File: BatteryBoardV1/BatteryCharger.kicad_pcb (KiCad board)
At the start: 2 copper layers, 49.5 x 50.8 mm, 12 parts, among them U1 MCP73213

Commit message: Add files via upload
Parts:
- removed PROG1: TP5, Wire_Pads:SolderWirePad_single_1-2mmDrill
- removed R3: 2.37K, Resistors_SMD:R_0603_HandSoldering
- removed STAT1: TP6, Wire_Pads:SolderWirePad_single_1-2mmDrill
- added Q1: Q_NMOS_GSD, TO_SOT_Packages_SMD:SOT-23, F.Cu at (142.2, 104.1)
- JIn1: footprint BJCs:DC_2.1mm_CUI-PJ-202A -> Connectors:Barrel_Jack_CUI_PJ-102AH
- R1: value 2.37K -> 1.185K
- moved R2 62.8 mm to (166.4, 98.4)
- moved JOut1 57.1 mm to (150.5, 109.9)
- moved JIn2 55.8 mm to (146.7, 82.5), turned to 0 degrees
- moved C1 54.3 mm to (142.2, 99.1)
- moved R1 54.3 mm to (158.1, 96.5)
- moved U1 54.2 mm to (150.5, 97.8)
- moved C2 54.0 mm to (141.6, 92.7)
- moved JIn1 50.0 mm to (165.7, 90.2)
- moved D1 39.4 mm to (150.5, 92.7), turned to 180 degrees
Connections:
- U1 pad 9: GND -> Net-(U1-Pad9)
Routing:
- net VDD: track 71.0 -> 5.75 mm, vias 0 -> 1
- net Net-(D1-Pad1): track 7.63 -> 20.1 mm
- net Net-(PROG1-Pad1): track 7.68 -> 0.00 mm
- net GND: track 33.1 -> 25.7 mm, vias 6 -> 10
- net Net-(R2-Pad1): track 19.7 -> 12.7 mm
- net Net-(R1-Pad1): track 8.64 -> 4.53 mm
- added copper zone on F.Cu, net VDD
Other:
- board size 49.5 x 50.8 mm -> 33.7 x 41.3 mm
- net class High Current added: clearance 0.2, trace_width 0.5, via_dia 0.6, via_drill 0.4
- net class Less High Current added: clearance 0.2, trace_width 0.3, via_dia 0.6, via_drill 0.4

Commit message: Add files via upload
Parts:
- added J1: Conn_01x04_Male, Connector_Molex:Molex_Micro-Fit_3.0_43045-0412_2x02_P3.00mm_Vertical, F.Cu at (153.4, 107.7)
- D1: footprint LEDs:LED_0603_HandSoldering -> LEDs:LED_0805_HandSoldering
- JIn2, JOut1: footprint Connectors_Terminal_Blocks:TerminalBlock_Altech_AK300-2_P5.00mm -> TerminalBlock_Phoenix:TerminalBlock_Phoenix_PT-1,5-2-5.0-H_1x02_P5.00mm_Horizontal
- R1: value 1.185K -> 3K; footprint Resistors_SMD:R_0603_HandSoldering -> Resistors_SMD:R_0805_HandSoldering
- R2: footprint Resistors_SMD:R_0603_HandSoldering -> Resistors_SMD:R_0805_HandSoldering
- U1: footprint Housings_SSOP:MSOP-10-1EP_3x3mm_Pitch0.5mm -> Housings_DFN_QFN:DFN-10-1EP_3x3mm_Pitch0.5mm
- moved JIn2 15.4 mm to (132.1, 87.4)
- moved U1 13.0 mm to (137.7, 100.1)
- moved R2 12.6 mm to (153.9, 100.6)
- moved C1 12.4 mm to (130.0, 101.1)
- moved Q1 12.1 mm to (130.6, 107.2)
- moved C2 11.9 mm to (130.0, 95.5)
- moved R1 11.5 mm to (146.8, 98.6)
- moved D1 9.68 mm to (141.2, 95.5)
- moved JIn1 9.55 mm to (156.5, 87.9), turned to 270 degrees
- moved JOut1 8.81 mm to (141.7, 110.7), turned to 180 degrees
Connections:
- net Net-(C1-Pad1) renamed /VBAT+
- JOut1 pad 2: GND -> /VBAT-
- Q1 pad 3: GND -> /VBAT-
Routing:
- net /VBAT+: track 20.2 -> 32.1 mm
- net /VBAT-: track 0.00 -> 8.14 mm
- net GND: track 25.7 -> 21.0 mm, vias 10 -> 13
- net VDD: track 5.75 -> 2.00 mm
- net Net-(D1-Pad1): track 20.1 -> 17.0 mm
- net Net-(R1-Pad1): track 4.53 -> 6.46 mm
- net Net-(R2-Pad1): track 12.7 -> 13.4 mm
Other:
- board size 33.7 x 41.3 mm -> 32.5 x 33.5 mm

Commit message: Add files via upload
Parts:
- J1: footprint Connector_Molex:Molex_Micro-Fit_3.0_43045-0412_2x02_P3.00mm_Vertical -> SOAR_Library:Molex_Micro-Fit_3.0_43045-0400_2x02_P3.00mm_Horizontal
- moved JIn1 14.3 mm to (142.2, 89.4), turned to 90 degrees
- moved J1 8.87 mm to (151.4, 116.3), turned to 0 degrees
- moved R2 6.78 mm to (147.3, 102.1)
- moved JOut1 4.82 mm to (137.2, 109.2), turned to 0 degrees
- moved D1 3.56 mm to (137.7, 95.5)
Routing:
- net /VBAT+: track 32.1 -> 3.44 mm, vias 0 -> 1
- net /VBAT-: track 8.14 -> 19.3 mm
- net VDD: track 2.00 -> 10.3 mm, vias 1 -> 2
- net Net-(R2-Pad1): track 13.4 -> 7.39 mm
- net Net-(D1-Pad1): track 17.0 -> 20.9 mm
- added copper zone on F.Cu, net /VBAT+
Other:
- board size 32.5 x 33.5 mm -> 30.5 x 34.5 mm

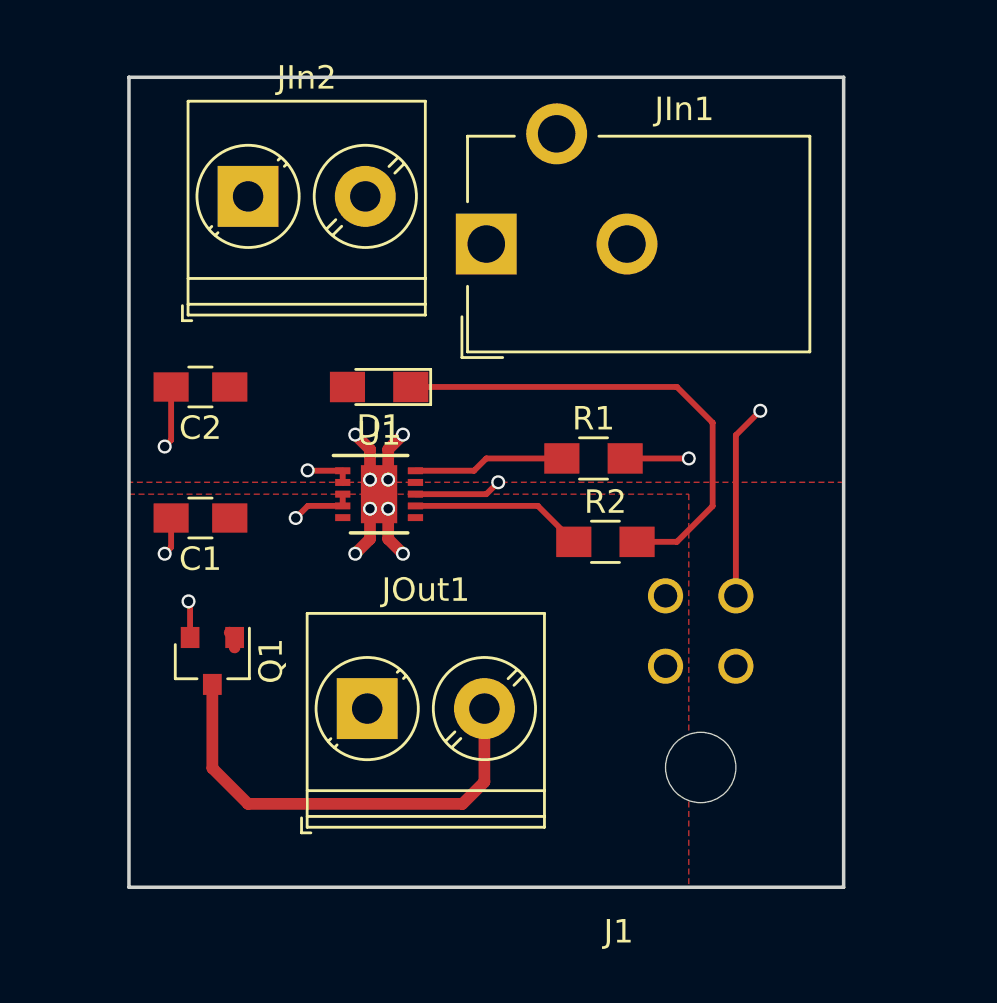
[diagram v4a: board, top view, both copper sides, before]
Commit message: Rearrange components to add mounting holes and silkscreen
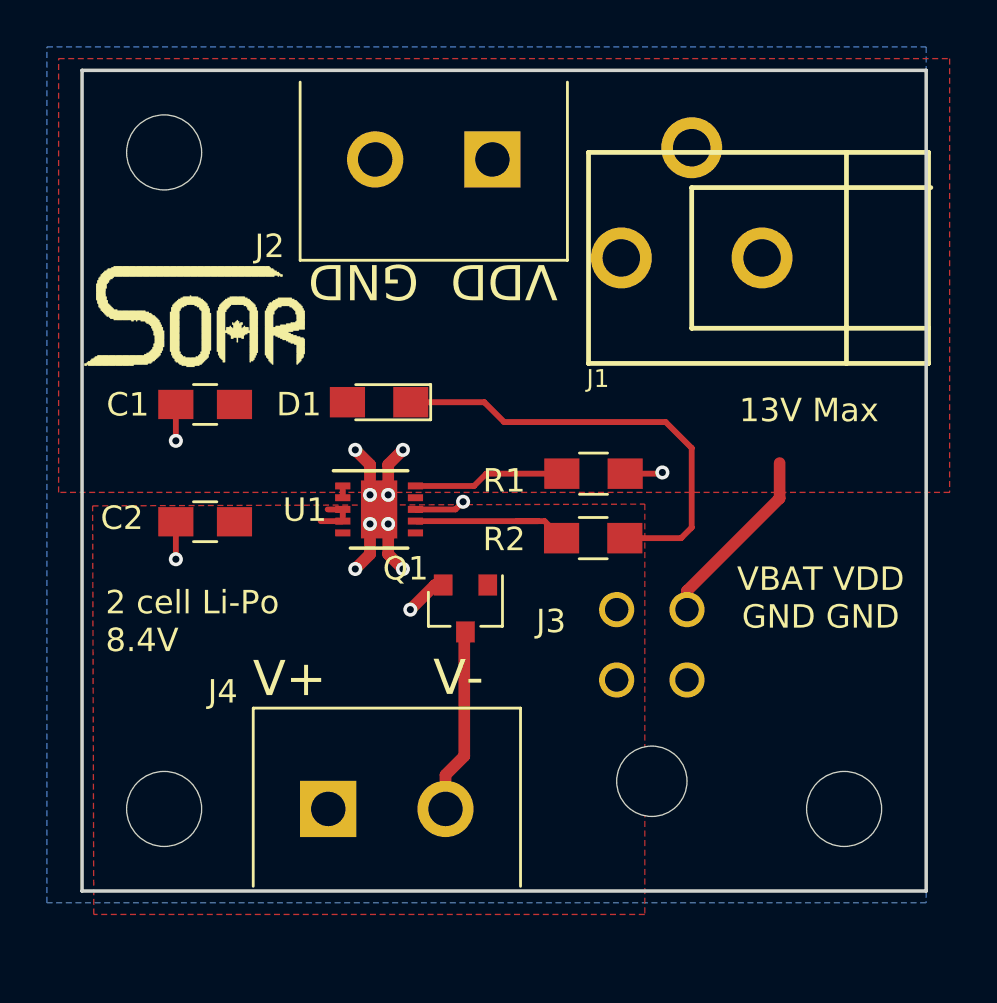
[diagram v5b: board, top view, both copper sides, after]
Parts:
- removed JIn1: Barrel_Jack, Connectors:Barrel_Jack_CUI_PJ-102AH
- removed JIn2: Input Terms., TerminalBlock_Phoenix:TerminalBlock_Phoenix_PT-1,5-2-5.0-H_1x02_P5.00mm_Horizontal
- removed JOut1: Bat.Terms., TerminalBlock_Phoenix:TerminalBlock_Phoenix_PT-1,5-2-5.0-H_1x02_P5.00mm_Horizontal
- added J2: Input Terms., SOAR_Kicad_Library:TerminalBlock_5mm_2POS_ED2600, F.Cu at (142.5, 85.8)
- added J3: Conn_01x04_Male, SOAR_Kicad_Library:Molex_Micro-Fit_3.0_43045-0400_2x02_P3.00mm_Horizontal, F.Cu at (149.3, 116.9)
- added J4: Bat.Terms., SOAR_Kicad_Library:TerminalBlock_5mm_2POS_ED2600, F.Cu at (135.5, 113.5)
- added LOGO_SOAR: , SOAR_Kicad_Library:LOGO_SOAR, F.Cu at (124.0, 89.5)
- added MK1: Mounting_Hole, Mounting_Holes:MountingHole_3.2mm_M3, F.Cu at (128.5, 113.5)
- added MK2: Mounting_Hole, Mounting_Holes:MountingHole_3.2mm_M3, F.Cu at (128.5, 85.5)
- added MK3: Mounting_Hole, Mounting_Holes:MountingHole_3.2mm_M3, F.Cu at (157.5, 113.5)
- J1: value Conn_01x04_Male -> Barrel_Jack; footprint SOAR_Library:Molex_Micro-Fit_3.0_43045-0400_2x02_P3.00mm_Horizontal -> SOAR_Kicad_Library:CUI_PJ-102A_2.5mm_DC_JACK
- moved J1 26.3 mm to (151.0, 90.0), turned to 270 degrees
- moved Q1 11.0 mm to (141.3, 105.0)
- moved C2 5.75 mm to (130.2, 101.2)
- moved C1 4.85 mm to (130.2, 96.2)
- moved U1 0.65 mm to (137.7, 100.7)
- moved D1 0.65 mm to (137.7, 96.2)
- moved R1 0.65 mm to (146.8, 99.2)
- moved R2 0.54 mm to (146.8, 102.0)
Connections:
- C1 pad 1: /VBAT+ -> VDD
- C2 pad 1: VDD -> /VBAT+
- J1 pad 1: GND -> VDD
- J1 pad 3: VDD -> GND
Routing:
- net /VBAT-: track 19.3 -> 8.24 mm
- net GND: track 21.0 -> 17.5 mm
- net VDD: track 10.3 -> 8.39 mm, vias 2 -> 0
- net Net-(D1-Pad1): track 20.9 -> 19.2 mm
- net /VBAT+: track 3.44 -> 2.09 mm, vias 1 -> 0
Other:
- board size 30.5 x 34.5 mm -> 36 x 35 mm
- net class Default: via_drill 0.4 -> 0.3
- net class High Current: via_drill 0.4 -> 0.3
- net class Less High Current: via_drill 0.4 -> 0.3
- board text added: "13V Max"
- board text added: "2 cell Li-Po 8.4V"
- board text added: "GND"
- board text added: "V+"
- board text added: "V-"
- board text added: "VBAT VDD GND GND"
- board text added: "VDD"

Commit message: final design published. Gerbers and schematic PDF generated.
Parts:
- removed Q1: Q_NMOS_GSD, TO_SOT_Packages_SMD:SOT-23
- LOGO_SOAR: moved to B.Cu
- moved LOGO_SOAR 15.6 mm to (126.5, 104.9)
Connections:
- J4 pad 2: /VBAT- -> GND
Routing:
- net VDD: track 8.39 -> 22.1 mm
- net /VBAT-: track 8.24 -> 0.00 mm
- net GND: track 17.5 -> 16.4 mm, vias 13 -> 12
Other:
- board text added: "Battery Board V1 (May 2018)"
